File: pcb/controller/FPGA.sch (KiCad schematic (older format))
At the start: 19 parts

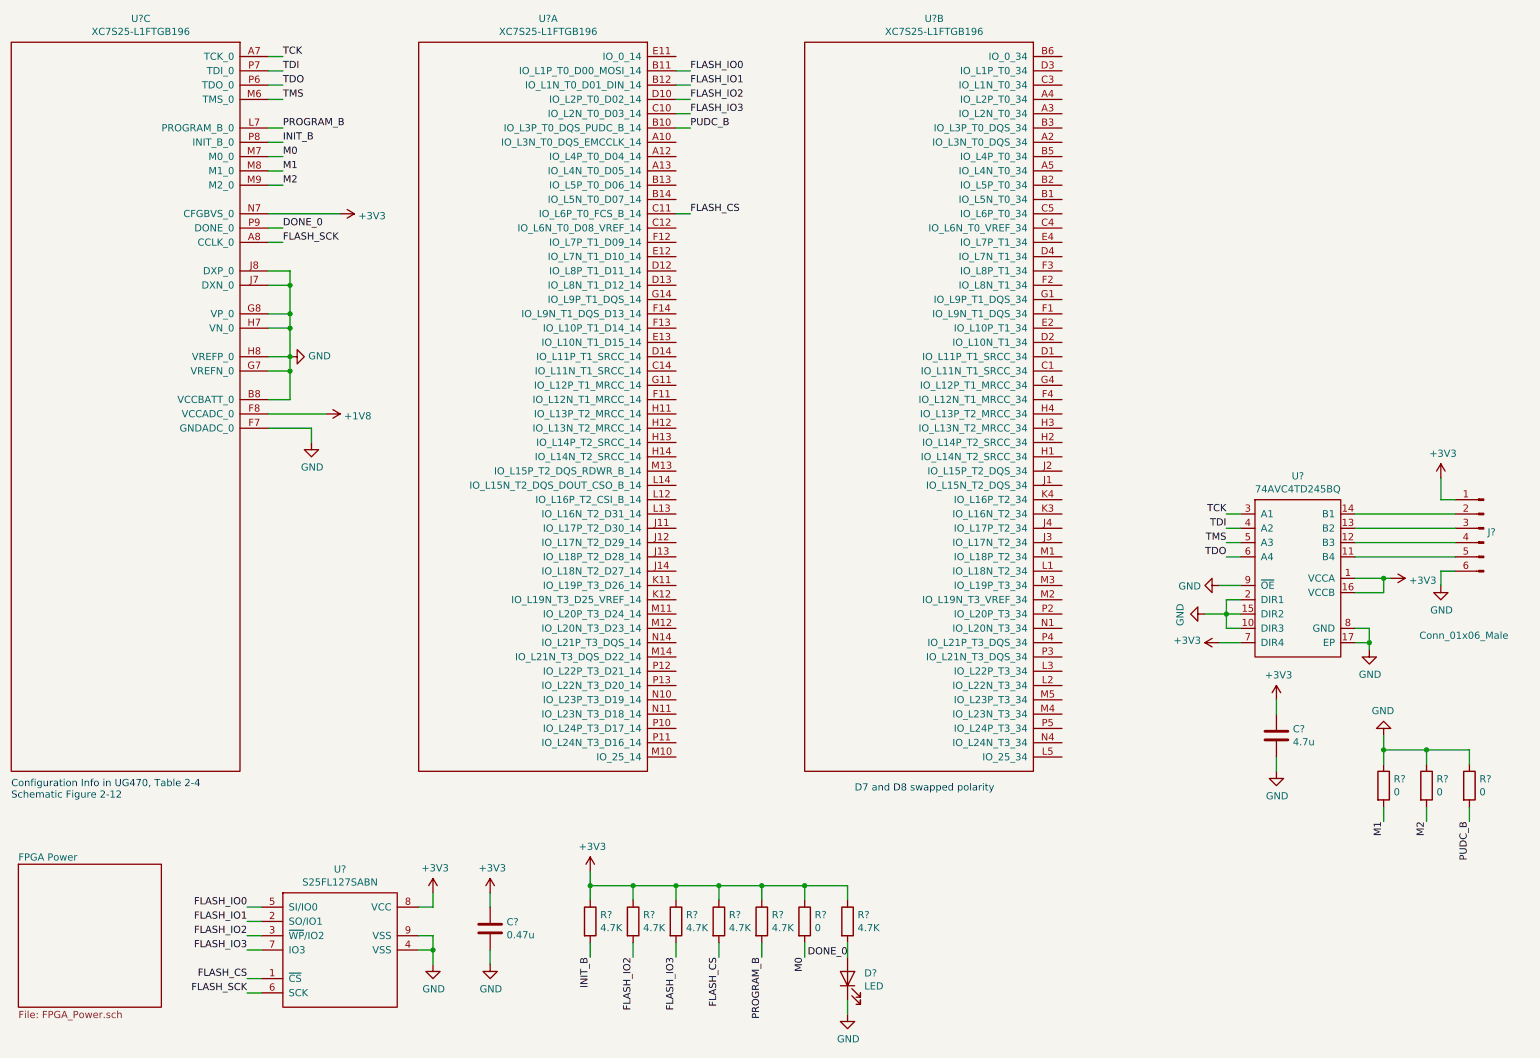
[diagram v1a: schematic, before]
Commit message: started assigning footprints
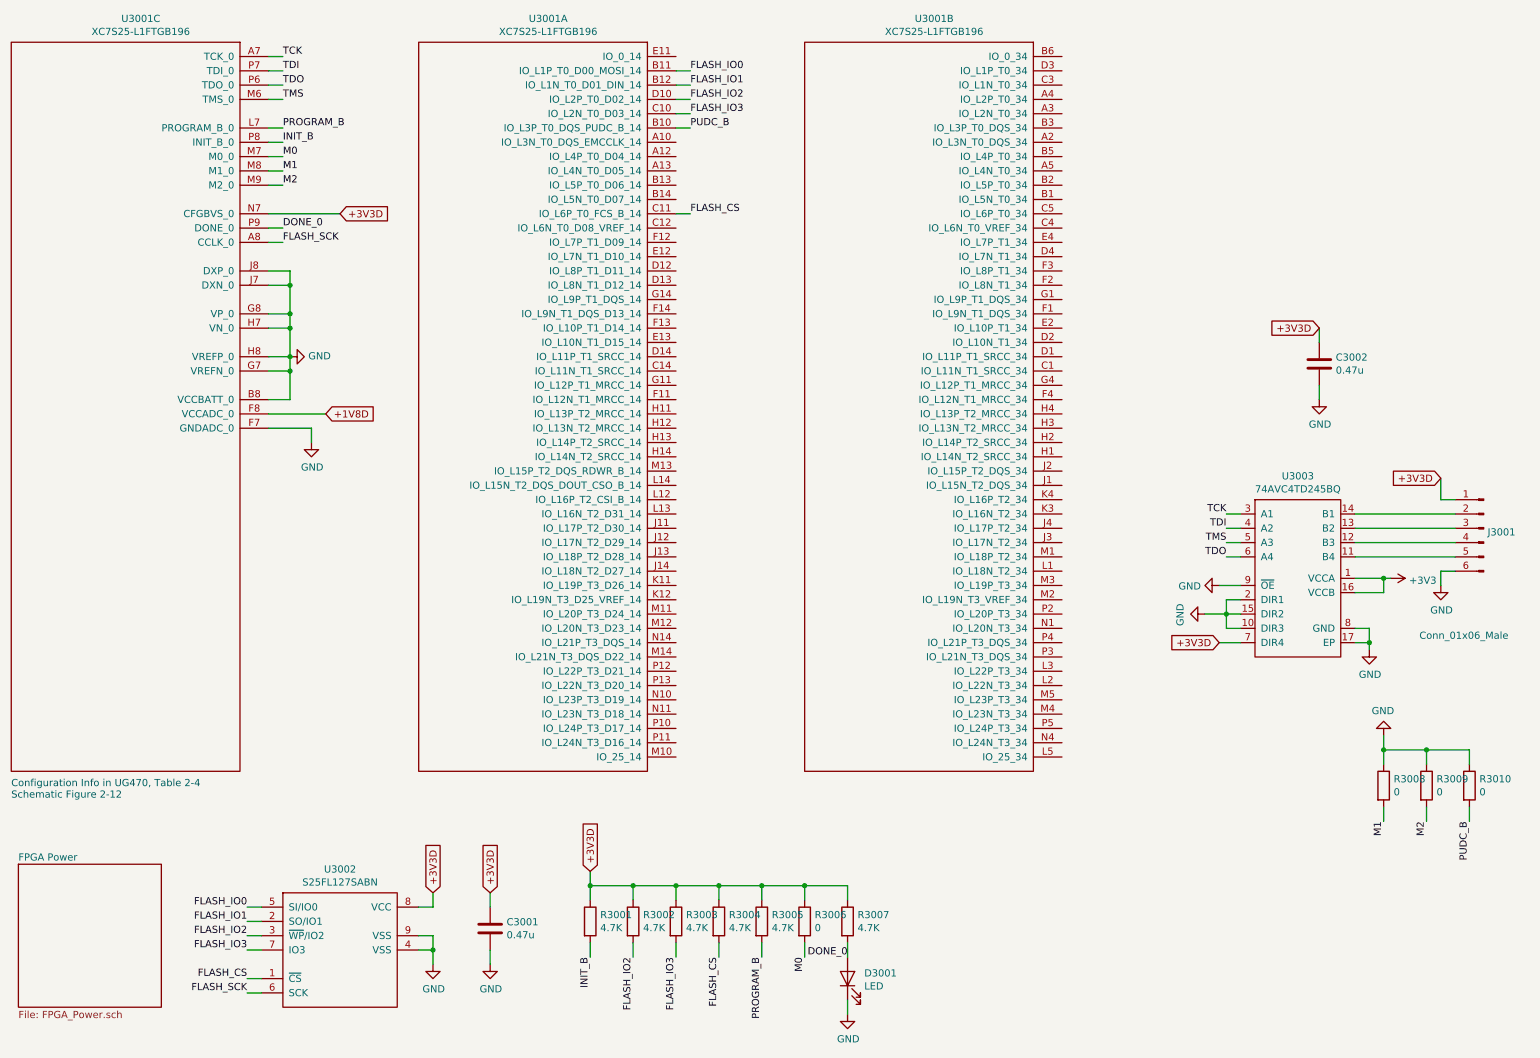
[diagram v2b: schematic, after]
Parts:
- C3002: renamed from C?; value 4.7u -> 0.47u
- gave numbers to parts that had none: 16
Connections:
- net +3V3: no longer C3001.1, C3002.1, J3001.1 (Pin_1), R3001.1, R3002.1, R3003.1, R3004.1, R3005.1, R3006.1, R3007.1, U3001.N7 (CFGBVS_0), U3002.8 (VCC), U3003.7 (DIR4)
- net +1V8 renamed +1V8D
- new net +3V3D: C3001.1, C3002.1, J3001.1 (Pin_1), R3001.1, R3002.1, R3003.1, R3004.1, R3005.1, R3006.1, R3007.1, U3001.N7 (CFGBVS_0), U3002.8 (VCC), U3003.7 (DIR4)
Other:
- note removed: "D7 and D8 swapped polarity"
- moved on the sheet: C3002

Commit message: pcb component placement almost done
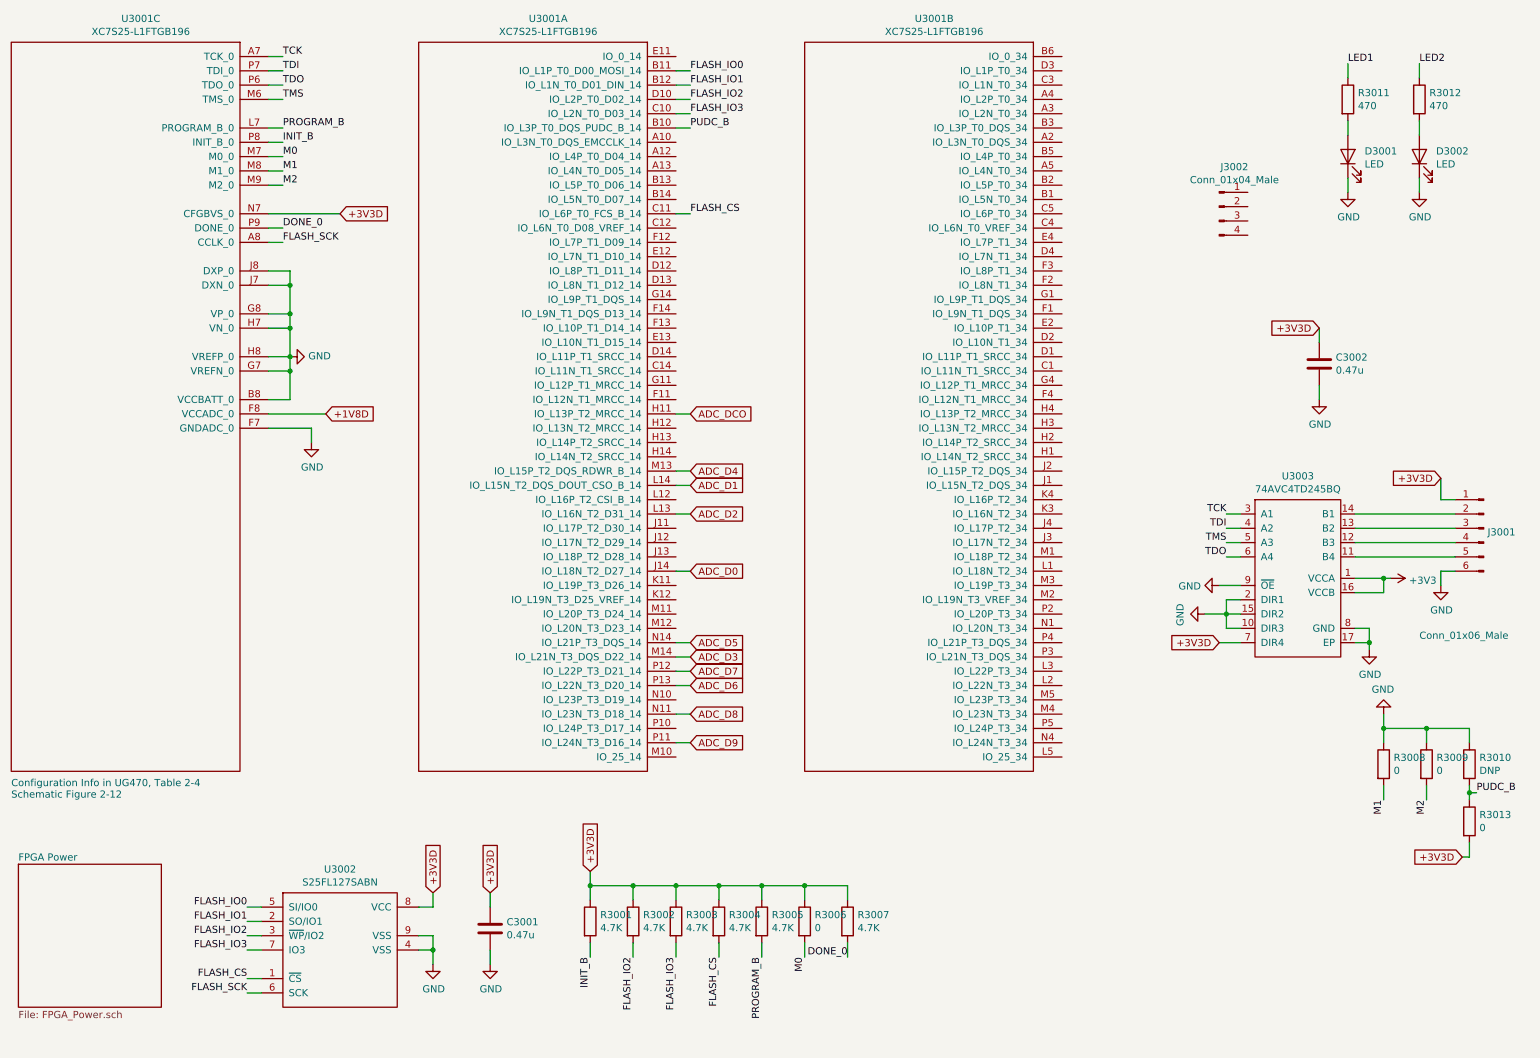
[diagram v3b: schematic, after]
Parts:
- added D3002: LED, wbraun_smd:LED-T1-RIGHT-ANGLE_4.6x4.4mm, symbol Device:LED
- added J3002: Conn_01x04_Male, Connector_PinHeader_2.54mm:PinHeader_1x04_P2.54mm_Vertical, symbol Connector:Conn_01x04_Male
- added R3011, R3012: 470, Resistor_SMD:R_0402_1005Metric, symbol Device:R
- added R3013: 0, Resistor_SMD:R_0402_1005Metric, symbol Device:R
- D3001: footprint LED_SMD:LED_0603_1608Metric -> wbraun_smd:LED-T1-RIGHT-ANGLE_4.6x4.4mm
- R3010: value 0 -> DNP
- U3002: footprint Package_SON:WSON-8-1EP_6x5mm_P1.27mm_EP3.4x4mm -> wbraun_smd:WSON-8-1EP_6x5mm_P1.27mm_EP3.4x4mm
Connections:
- net +3V3D: now also R3013.2
- net DONE_0: no longer D3001.2 (A)
- net GND: now also D3002.1 (K)
- net PUDC_B: now also R3013.1
- net ADC_DCO: now reaches U3001.H11 (IO_L13P_T2_MRCC_14)
- net ADC_D0: now reaches U3001.J14 (IO_L18N_T2_D27_14)
- net ADC_D2: now reaches U3001.L13 (IO_L16N_T2_D31_14)
- net ADC_D1: now reaches U3001.L14 (IO_L15N_T2_DQS_DOUT_CSO_B_14)
- net ADC_D4: now reaches U3001.M13 (IO_L15P_T2_DQS_RDWR_B_14)
- net ADC_D3: now reaches U3001.M14 (IO_L21N_T3_DQS_D22_14)
- net ADC_D8: now reaches U3001.N11 (IO_L23N_T3_D18_14)
- net ADC_D5: now reaches U3001.N14 (IO_L21P_T3_DQS_14)
- net ADC_D9: now reaches U3001.P11 (IO_L24N_T3_D16_14)
- net ADC_D7: now reaches U3001.P12 (IO_L22P_T3_D21_14)
- net ADC_D6: now reaches U3001.P13 (IO_L22N_T3_D20_14)
- new net: D3002.2 (A), R3012.2
- new net: D3001.2 (A), R3011.2
- new net LED1: R3011.1
- new net LED2: R3012.1
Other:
- moved on the sheet: R3008, R3009, R3010

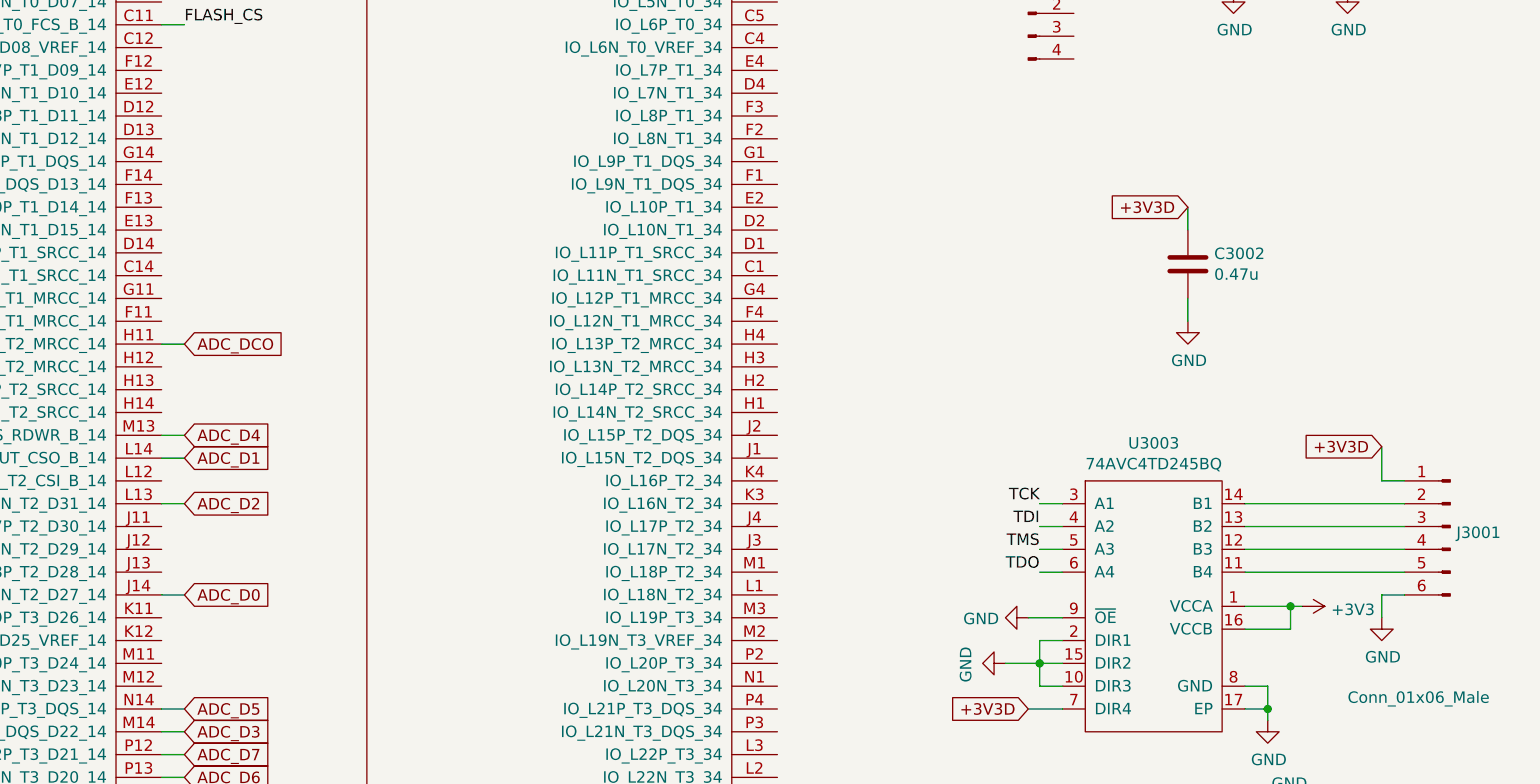
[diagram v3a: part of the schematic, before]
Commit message: controller PCB routing progress
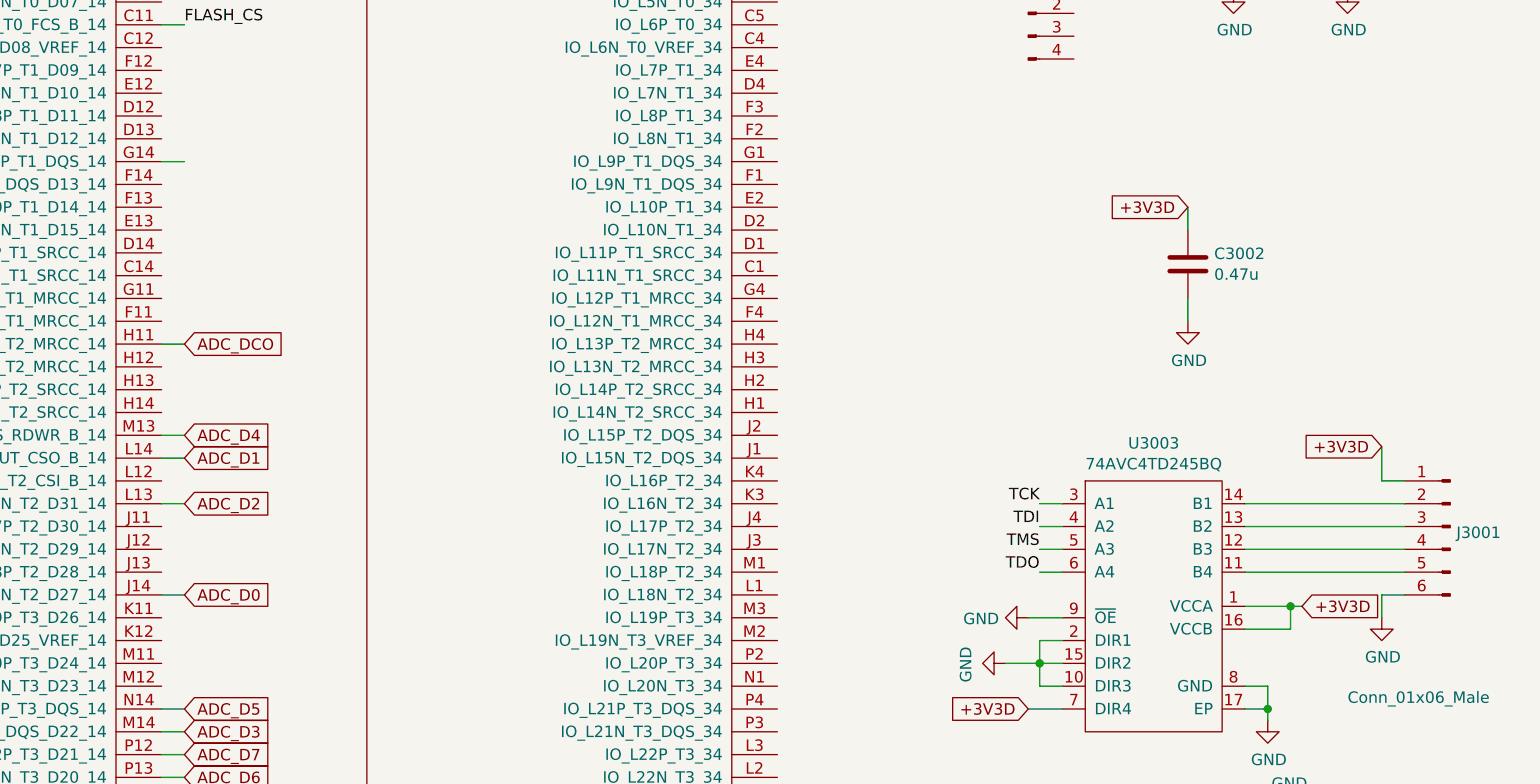
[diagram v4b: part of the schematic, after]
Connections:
- net +3V3 is gone; now on net +3V3D: U3003.1 (VCCA), U3003.16 (VCCB)
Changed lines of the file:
@@
 Connection ~ 10250 4500
-$Comp
-L power:+3V3 #PWR0136
-U 1 1 5C0E65BD
-P 10300 4500
-F 0 "#PWR0136" H 10300 4350 50  0001 C CNN
-F 1 "+3V3" V 10315 4628 50  0000 L CNN
-F 2 "" H 10300 4500 50  0001 C CNN
-F 3 "" H 10300 4500 50  0001 C CNN
-	1    10300 4500
-	0    1    1    0
-$EndComp
 $Comp
 L power:GND #PWR0137
@@
 	1    0    0    -1
 $EndComp
+Wire Wire Line
+	5300 2550 5400 2550
+Text GLabel 10300 4500 2    50   Input ~ 0
++3V3D
 $EndSCHEMATC

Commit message: routing almost done
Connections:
- net +3V3D: now also J3002.1 (Pin_1)
- net GND: now also J3002.4 (Pin_4)
- net LED1: now also U3001.J13 (IO_L18P_T2_D28_14)
- net LED2: now also U3001.J12 (IO_L17N_T2_D29_14)
- net GATE_1: now reaches U3001.B14 (IO_L5N_T0_D07_14)
- net GATE_2: now reaches U3001.D14 (IO_L11P_T1_SRCC_14)
- net GATE_3: now reaches U3001.F14 (IO_L9N_T1_DQS_D13_14)
- net DEBUG_TX: now reaches U3001.G14 (IO_L9P_T1_DQS_14)
- net DEBUG_TX: now also J3002.2 (Pin_2)
- net DEBUG_RX: now reaches U3001.H12 (IO_L13N_T2_MRCC_14)
- net DEBUG_RX: now also J3002.3 (Pin_3)
- net UVLO: now reaches U3001.H13 (IO_L14P_T2_SRCC_14)
- net GATE_4: now reaches U3001.H14 (IO_L14N_T2_SRCC_14)
- net ZCS_DETECT: now reaches U3001.K12 (IO_L19N_T3_D25_VREF_14)
- net FIBER_TX: now reaches U3001.B1 (IO_L5N_T0_34)
- net FIBER_RX: now reaches U3001.C1 (IO_L11N_T1_SRCC_34)
- net ADC_MODE: now reaches U3001.M1 (IO_L18P_T2_34)
- net ADC_SDIO: now reaches U3001.N1 (IO_L20N_T3_34)
- net ADC_SCLK: now reaches U3001.P2 (IO_L20P_T3_34)
- net ADC_CSB: now reaches U3001.P3 (IO_L21N_T3_DQS_34)
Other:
- moved on the sheet: J3002
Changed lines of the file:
@@
 L Connector:Conn_01x04_Male J3002
 U 1 1 5C4F5670
-P 9100 1900
-F 0 "J3002" H 9206 2178 50  0000 C CNN
-F 1 "Conn_01x04_Male" H 9206 2087 50  0000 C CNN
-F 2 "Connector_PinHeader_2.54mm:PinHeader_1x04_P2.54mm_Vertical" H 9100 1900 50  0001 C CNN
-F 3 "~" H 9100 1900 50  0001 C CNN
-	1    9100 1900
+P 9400 1900
+F 0 "J3002" H 9506 2178 50  0000 C CNN
+F 1 "Conn_01x04_Male" H 9506 2087 50  0000 C CNN
+F 2 "Connector_PinHeader_2.54mm:PinHeader_1x04_P2.54mm_Vertical" H 9400 1900 50  0001 C CNN
+F 3 "~" H 9400 1900 50  0001 C CNN
+	1    9400 1900
+	-1   0    0    -1
+$EndComp
+Text GLabel 10300 4500 2    50   Input ~ 0
++3V3D
+Wire Wire Line
+	5300 1850 5400 1850
+Text GLabel 5400 1850 2    50   Input ~ 0
+GATE_1
+Wire Wire Line
+	5300 2950 5400 2950
+Text GLabel 5400 2950 2    50   Input ~ 0
+GATE_2
+Wire Wire Line
+	5300 2650 5400 2650
+Text GLabel 5400 2650 2    50   Input ~ 0
+GATE_3
+Wire Wire Line
+	5300 3650 5400 3650
+Text GLabel 5400 3650 2    50   Input ~ 0
+GATE_4
+Wire Wire Line
+	8000 4850 8100 4850
+Wire Wire Line
+	8000 3050 8100 3050
+Wire Wire Line
+	8000 1850 8100 1850
+Text GLabel 8100 1850 2    50   Input ~ 0
+FIBER_TX
+Text GLabel 8100 3050 2    50   Input ~ 0
+FIBER_RX
+Wire Wire Line
+	8000 4350 8100 4350
+Wire Wire Line
+	9200 1800 9100 1800
+Wire Wire Line
+	9200 2100 9100 2100
+Wire Wire Line
+	9200 2000 9100 2000
+Wire Wire Line
+	9200 1900 9100 1900
+Text GLabel 9100 1700 0    50   Input ~ 0
++3V3D
+Wire Wire Line
+	9100 1700 9100 1800
+Wire Wire Line
+	9100 2100 9100 2200
+$Comp
+L power:GND #PWR?
+U 1 1 5C4ECF97
+P 9100 2200
+F 0 "#PWR?" H 9100 1950 50  0001 C CNN
+F 1 "GND" H 9105 2027 50  0000 C CNN
+F 2 "" H 9100 2200 50  0001 C CNN
+F 3 "" H 9100 2200 50  0001 C CNN
+	1    9100 2200
 	1    0    0    -1
 $EndComp
+Text Label 9100 1900 2    50   ~ 0
+DEBUG_TX
+Text Label 9100 2000 2    50   ~ 0
+DEBUG_RX
+Wire Wire Line
+	5300 3550 5400 3550
+Text GLabel 5400 4650 2    50   Input ~ 0
+ZCS_DETECT
+Wire Wire Line
+	8000 5050 8100 5050
+Text GLabel 8100 5050 2    50   Input ~ 0
+ADC_CSB
+Wire Wire Line
+	8000 4750 8100 4750
+Text GLabel 8100 4750 2    50   Input ~ 0
+ADC_SCLK
+Text GLabel 8100 4850 2    50   Input ~ 0
+ADC_SDIO
+Text GLabel 8100 4350 2    50   Input ~ 0
+ADC_MODE
+Wire Wire Line
+	5300 4650 5400 4650
+Text GLabel 5400 3550 2    50   Input ~ 0
+UVLO
+Wire Wire Line
+	5300 3450 5400 3450
+Text Label 5400 3450 0    50   ~ 0
+DEBUG_RX
 Wire Wire Line
 	5300 2550 5400 2550
-Text GLabel 10300 4500 2    50   Input ~ 0
-+3V3D
+Text Label 5400 2550 0    50   ~ 0
+DEBUG_TX
+Wire Wire Line
+	5300 4350 5400 4350
+Text Label 5400 4350 0    50   ~ 0
+LED1
+Wire Wire Line
+	5300 4250 5400 4250
+Text Label 5400 4250 0    50   ~ 0
+LED2
 $EndSCHEMATC
